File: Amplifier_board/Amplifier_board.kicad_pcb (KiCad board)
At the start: 2 copper layers, 100 x 100 mm, 125 parts, among them J1 Screw Terminal, J10 Conn_01x03_Pin, J11 Conn_01x03_Pin, J12 Conn_01x03_Pin, J13 Conn_01x03_Pin, J14 Conn_01x03_Pin, J15 Conn_01x03_Pin, J2 Screw Terminal, J3 Screw Terminal, J4 Screw Terminal, J5 Screw Terminal, J6 Screw Terminal, J7 A-DF_09_A_KG-T4S, J8 Conn_01x03_Pin, J9 Conn_01x03_Pin, U1 TPA3111D1PWPR, U2 TPA3111D1PWPR, U3 TPA3111D1PWPR, U4 TPA3111D1PWPR

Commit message: More progress on layout
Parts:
- C17, C3, C32, C4, C47: moved to B.Cu
- C28, C29, C43, C44, C54, C58, C60, C61: value 0.5u -> 0.47u
- moved J5 19.0 mm to (162.0, 134.5)
- moved J4 16.0 mm to (137.0, 134.5)
- moved J3 12.5 mm to (112.0, 134.5)
- moved C1 10.2 mm to (88.2, 79.3), turned to 180 degrees
- moved C2 5.91 mm to (88.2, 81.8), turned to 0 degrees
- moved C4 5.46 mm to (84.3, 90.9), turned to 0 degrees
- moved C63 4.20 mm to (215.9, 103.6)
- moved C64 4.20 mm to (199.4, 166.7)
- moved C65 4.20 mm to (269.3, 141.6)
- moved C67 4.20 mm to (210.9, 103.6)
- moved C68 4.20 mm to (194.4, 166.7)
- moved C69 4.20 mm to (264.3, 141.6)
- moved R13 4.00 mm to (84.5, 122.5)
- moved R9 4.00 mm to (89.5, 122.5)
- moved C18 3.21 mm to (212.1, 65.5), turned to -90 degrees
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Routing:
- net +24V: track 0.00 -> 328.3 mm, vias 0 -> 9
- net Net-(U1-INP): track 0.00 -> 12.7 mm
- net Net-(U1-INN): track 0.00 -> 9.94 mm
- net Net-(U4-*FAULT): track 0.00 -> 7.07 mm
- net Net-(U2-*FAULT): track 0.00 -> 7.07 mm
- net Net-(U3-*FAULT): track 0.00 -> 7.07 mm
- net Net-(C61-Pad1): track 0.00 -> 6.03 mm
- net Net-(C44-Pad1): track 0.00 -> 6.03 mm
- net Net-(C29-Pad1): track 0.00 -> 6.03 mm
- net Net-(C58-Pad1): track 0.00 -> 5.98 mm
- net Net-(C54-Pad2): track 0.00 -> 5.98 mm
- net Net-(C28-Pad2): track 0.00 -> 5.98 mm
- net Net-(C43-Pad2): track 0.00 -> 5.98 mm
- net Net-(C60-Pad2): track 0.00 -> 5.98 mm
- net Net-(U3-GVDD): track 0.00 -> 4.85 mm
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
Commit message: More routing on amp board
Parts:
- added JP10: Jumper_1206, Resistor_SMD:R_1206_3216Metric_Pad1.30x1.75mm_HandSolder, F.Cu at (54.0, 60.9)
- added JP11: Jumper_1206, Resistor_SMD:R_1206_3216Metric_Pad1.30x1.75mm_HandSolder, F.Cu at (46.0, 60.9)
- added JP12: Jumper_1206, Resistor_SMD:R_1206_3216Metric_Pad1.30x1.75mm_HandSolder, F.Cu at (46.0, 52.3)
- added JP13: Jumper_1206, Resistor_SMD:R_1206_3216Metric_Pad1.30x1.75mm_HandSolder, F.Cu at (89.0, 79.5)
- added JP14: Jumper_1206, Resistor_SMD:R_1206_3216Metric_Pad1.30x1.75mm_HandSolder, F.Cu at (54.0, 64.2)
- added JP15: Jumper_1206, Resistor_SMD:R_1206_3216Metric_Pad1.30x1.75mm_HandSolder, F.Cu at (46.0, 64.2)
- added JP16: Jumper_1206, Resistor_SMD:R_1206_3216Metric_Pad1.30x1.75mm_HandSolder, F.Cu at (46.0, 55.6)
- added JP9: Jumper_1206, Resistor_SMD:R_1206_3216Metric_Pad1.30x1.75mm_HandSolder, F.Cu at (91.6, 79.5)
- moved C1 6.26 mm to (83.3, 83.2), turned to -90 degrees
- moved C2 3.04 mm to (85.5, 83.2), turned to 90 degrees
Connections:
- J10 pad 2: /amp3/Gain0 -> Net-(J10-Pin_2)
- J11 pad 2: /amp4/Gain0 -> Net-(J11-Pin_2)
- J12 pad 2: /amp1/Gain1 -> Net-(J12-Pin_2)
- J13 pad 2: /amp2/Gain1 -> Net-(J13-Pin_2)
- J14 pad 2: /amp3/Gain1 -> Net-(J14-Pin_2)
- J15 pad 2: /amp4/Gain1 -> Net-(J15-Pin_2)
- J8 pad 2: /amp1/Gain0 -> Net-(J8-Pin_2)
- J9 pad 2: /amp2/Gain0 -> Net-(J9-Pin_2)
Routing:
- net /In1N: track 0.00 -> 46.7 mm
- net /In1P: track 0.00 -> 46.2 mm
- net Net-(J8-Pin_2): track 0.00 -> 11.4 mm
- net /amp1/Gain0: track 0.70 -> 10.9 mm
- net /amp1/Gain1: track 0.01 -> 10.1 mm
- net Net-(U1-INP): track 12.7 -> 6.81 mm
- net Net-(J12-Pin_2): track 0.00 -> 4.79 mm
- net +24V: track 328.3 -> 324.0 mm
- net Net-(U1-INN): track 9.94 -> 6.81 mm
- added copper zone on B.Cu, net GND

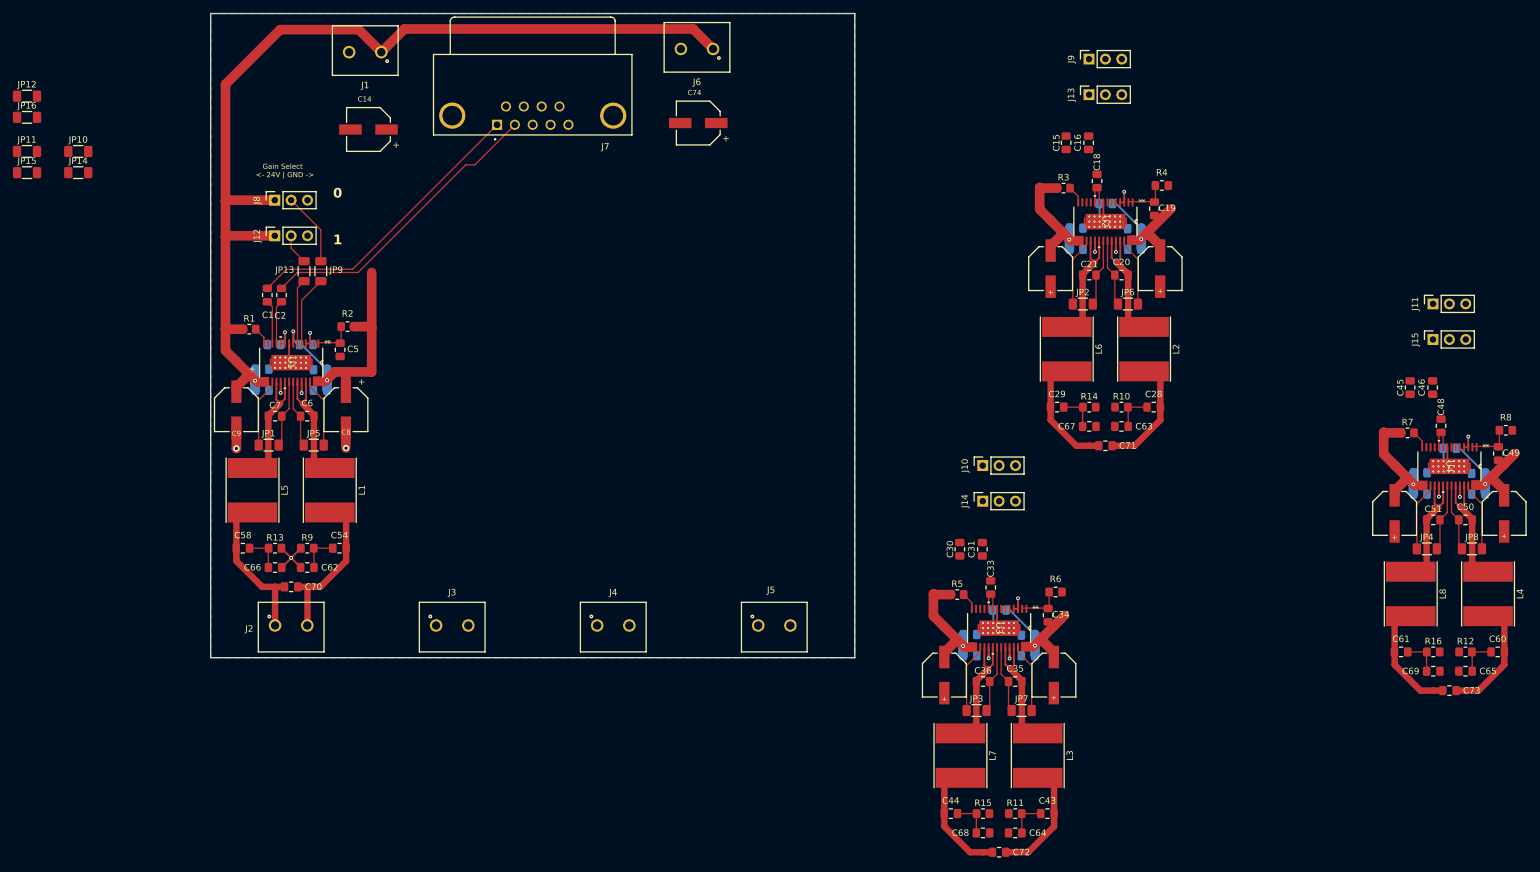
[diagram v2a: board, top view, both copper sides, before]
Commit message: Removed buffers on DAC board
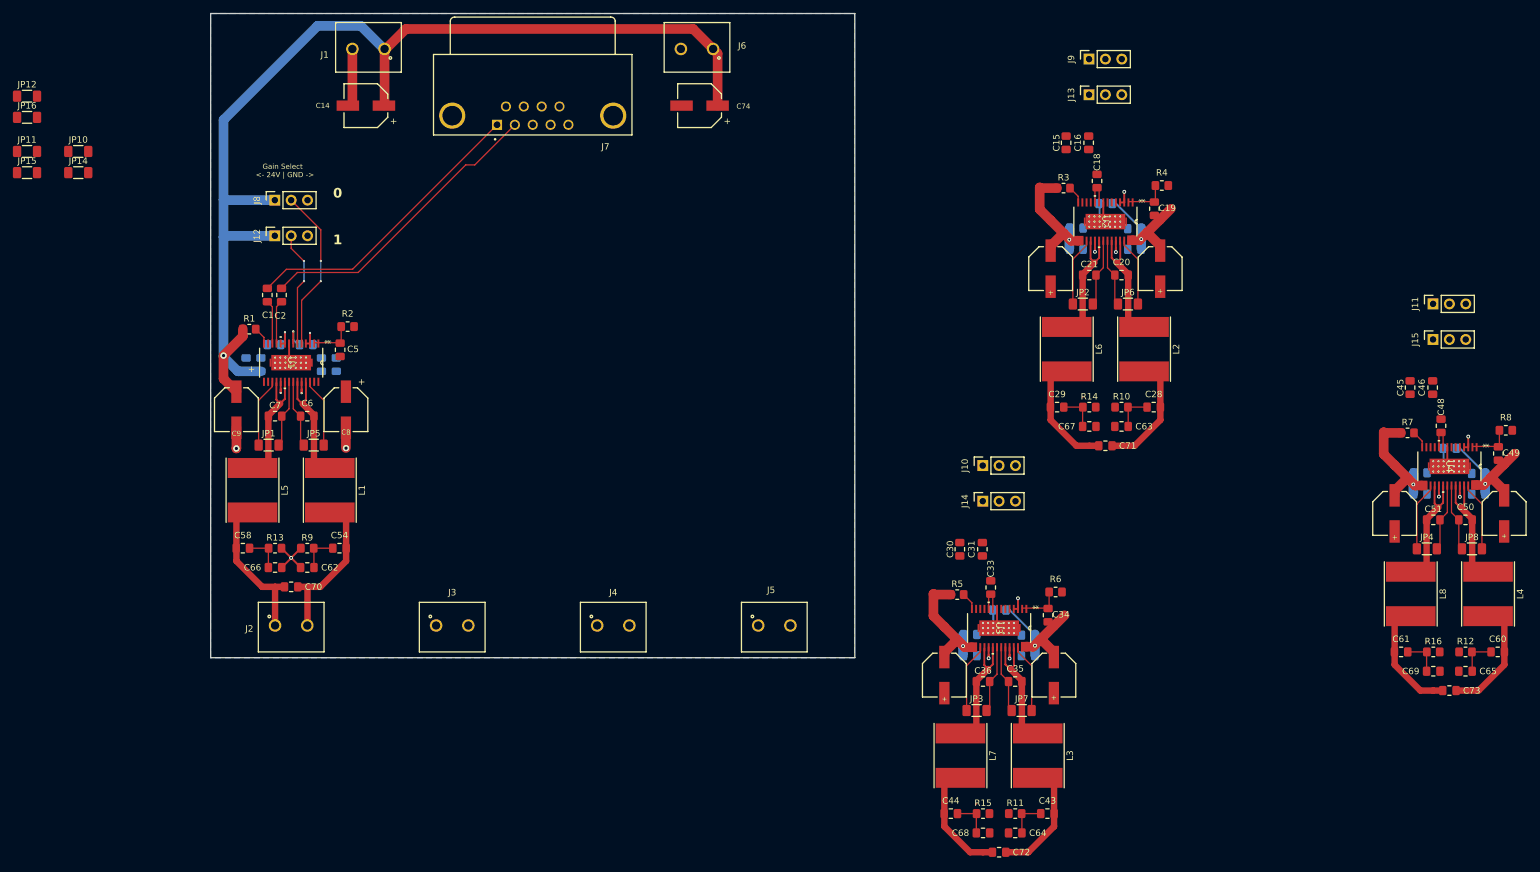
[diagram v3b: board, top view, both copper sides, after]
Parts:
- removed JP13, JP9: Jumper_1206, Resistor_SMD:R_1206_3216Metric_Pad1.30x1.75mm_HandSolder
- moved C12 4.00 mm to (82.3, 94.0), turned to 90 degrees
- moved C13 4.00 mm to (91.7, 94.0), turned to 90 degrees
- moved C14 3.72 mm to (98.6, 53.8)
- moved C74 2.71 mm to (150.4, 53.8)
- moved C11 2.62 mm to (94.0, 94.0), turned to 90 degrees
- moved C10 2.60 mm to (80.0, 94.0), turned to 90 degrees
- moved J1 0.71 mm to (99.0, 45.0)
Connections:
- C74 pad 1: unconnected-(C74-Pad1) -> +24V
- C74 pad 2: unconnected-(C74-Pad2) -> GND
- J10 pad 2: Net-(J10-Pin_2) -> /amp3/Gain0
- J11 pad 2: Net-(J11-Pin_2) -> /amp4/Gain0
- J12 pad 2: Net-(J12-Pin_2) -> /amp1/Gain1
- J13 pad 2: Net-(J13-Pin_2) -> /amp2/Gain1
- J14 pad 2: Net-(J14-Pin_2) -> /amp3/Gain1
- J15 pad 2: Net-(J15-Pin_2) -> /amp4/Gain1
- J8 pad 2: Net-(J8-Pin_2) -> /amp1/Gain0
- J9 pad 2: Net-(J9-Pin_2) -> /amp2/Gain0
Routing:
- net +24V: track 324.0 -> 303.5 mm, vias 9 -> 8
- net /amp1/Gain0: track 10.9 -> 25.4 mm, vias 0 -> 2
- net Net-(J8-Pin_2): track 11.4 -> 0.00 mm
- net GND: track 62.0 -> 70.0 mm
- net /amp1/Gain1: track 10.1 -> 18.0 mm, vias 0 -> 2
- net Net-(J12-Pin_2): track 4.79 -> 0.00 mm

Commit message: Added test points, almost finished layout for amp board
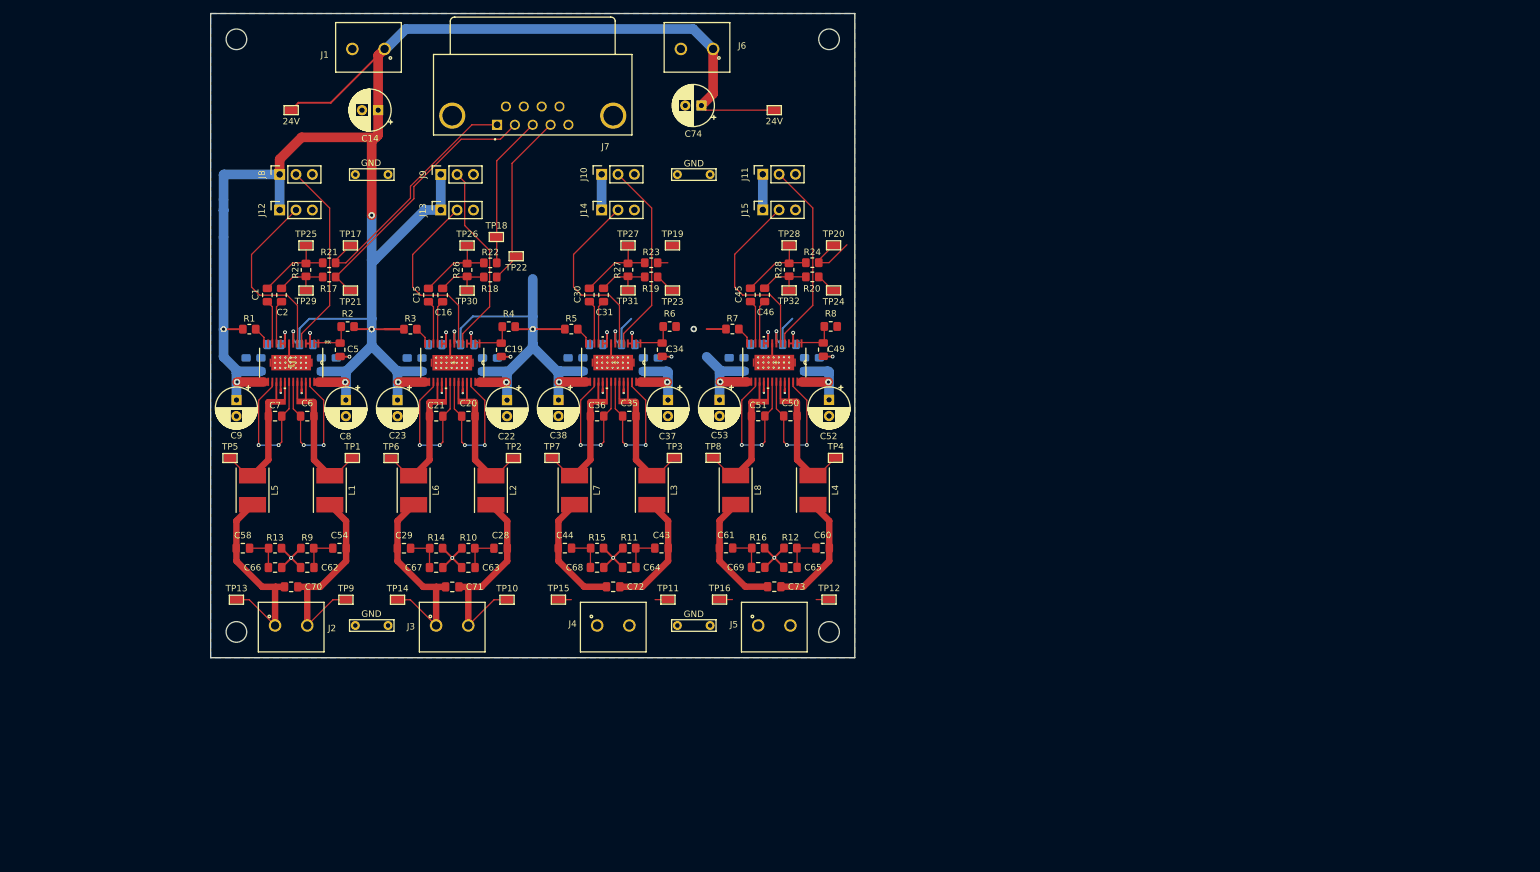
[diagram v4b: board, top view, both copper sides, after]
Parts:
- removed JP1, JP10, JP11, JP12, JP14, JP15, JP16, JP2, JP3, JP4, JP5, JP6, JP7, JP8: Jumper_1206, Resistor_SMD:R_1206_3216Metric_Pad1.30x1.75mm_HandSolder
- added R17: 0, Resistor_SMD:R_0805_2012Metric_Pad1.20x1.40mm_HandSolder, F.Cu at (92.9, 80.4)
- added R18: 0, Resistor_SMD:R_0805_2012Metric_Pad1.20x1.40mm_HandSolder, F.Cu at (117.9, 80.4)
- added R19: 0, Resistor_SMD:R_0805_2012Metric_Pad1.20x1.40mm_HandSolder, F.Cu at (142.9, 80.4)
- added R20: 0, Resistor_SMD:R_0805_2012Metric_Pad1.20x1.40mm_HandSolder, F.Cu at (167.9, 80.4)
- added R21: 0, Resistor_SMD:R_0805_2012Metric_Pad1.20x1.40mm_HandSolder, F.Cu at (92.9, 78.2)
- added R22: 0, Resistor_SMD:R_0805_2012Metric_Pad1.20x1.40mm_HandSolder, F.Cu at (117.9, 78.2)
- added R23: 0, Resistor_SMD:R_0805_2012Metric_Pad1.20x1.40mm_HandSolder, F.Cu at (142.9, 78.2)
- added R24: 0, Resistor_SMD:R_0805_2012Metric_Pad1.20x1.40mm_HandSolder, F.Cu at (167.9, 78.2)
- added R25: omit, Resistor_SMD:R_0805_2012Metric_Pad1.20x1.40mm_HandSolder, F.Cu at (89.3, 79.3)
- added R26: omit, Resistor_SMD:R_0805_2012Metric_Pad1.20x1.40mm_HandSolder, F.Cu at (114.3, 79.3)
- added R27: omit, Resistor_SMD:R_0805_2012Metric_Pad1.20x1.40mm_HandSolder, F.Cu at (139.3, 79.3)
- added R28: omit, Resistor_SMD:R_0805_2012Metric_Pad1.20x1.40mm_HandSolder, F.Cu at (164.3, 79.3)
- added TP1: N, project_lib:TP_RCUCTE, F.Cu at (96.5, 108.5)
- added TP10: OutN, project_lib:TP_RCUCTE, F.Cu at (120.5, 130.5)
- added TP11: OutN, project_lib:TP_RCUCTE, F.Cu at (145.5, 130.5)
- added TP12: OutN, project_lib:TP_RCUCTE, F.Cu at (170.5, 130.5)
- added TP13: OutP, project_lib:TP_RCUCTE, F.Cu at (78.5, 130.5)
- added TP14: OutP, project_lib:TP_RCUCTE, F.Cu at (103.5, 130.5)
- added TP15: OutP, project_lib:TP_RCUCTE, F.Cu at (128.5, 130.5)
- added TP16: OutP, project_lib:TP_RCUCTE, F.Cu at (153.5, 130.5)
- added TP17: InP, project_lib:TP_RCUCTE, F.Cu at (96.2, 75.5)
- added TP18: InP, project_lib:TP_RCUCTE, F.Cu at (118.8, 74.2)
- added TP19: InP, project_lib:TP_RCUCTE, F.Cu at (146.2, 75.5)
- added TP2: N, project_lib:TP_RCUCTE, F.Cu at (121.5, 108.5)
- added TP20: InP, project_lib:TP_RCUCTE, F.Cu at (171.2, 75.5)
- added TP21: InN, project_lib:TP_RCUCTE, F.Cu at (96.2, 82.5)
- added TP22: InN, project_lib:TP_RCUCTE, F.Cu at (121.9, 77.2)
- added TP23: InN, project_lib:TP_RCUCTE, F.Cu at (146.2, 82.5)
- added TP24: InN, project_lib:TP_RCUCTE, F.Cu at (171.2, 82.5)
- added TP25: P, project_lib:TP_RCUCTE, F.Cu at (89.3, 75.5)
- added TP26: P, project_lib:TP_RCUCTE, F.Cu at (114.3, 75.5)
- added TP27: P, project_lib:TP_RCUCTE, F.Cu at (139.3, 75.5)
- added TP28: P, project_lib:TP_RCUCTE, F.Cu at (164.3, 75.5)
- added TP29: N, project_lib:TP_RCUCTE, F.Cu at (89.3, 82.5)
- added TP3: N, project_lib:TP_RCUCTE, F.Cu at (146.5, 108.5)
- added TP30: N, project_lib:TP_RCUCTE, F.Cu at (114.3, 82.5)
- added TP31: N, project_lib:TP_RCUCTE, F.Cu at (139.3, 82.5)
- added TP32: N, project_lib:TP_RCUCTE, F.Cu at (164.3, 82.5)
- added TP33: 24V, project_lib:TP_RCUCTE, F.Cu at (87.0, 54.5)
- added TP34: 24V, project_lib:TP_RCUCTE, F.Cu at (162.0, 54.5)
- added TP35: GND, TestPoint:TestPoint_Bridge_Pitch5.08mm_Drill0.7mm, F.Cu at (97.0, 64.5)
- added TP36: GND, TestPoint:TestPoint_Bridge_Pitch5.08mm_Drill0.7mm, F.Cu at (97.0, 134.5)
- added TP37: GND, TestPoint:TestPoint_Bridge_Pitch5.08mm_Drill0.7mm, F.Cu at (147.0, 64.5)
- added TP38: GND, TestPoint:TestPoint_Bridge_Pitch5.08mm_Drill0.7mm, F.Cu at (147.0, 134.5)
- added TP4: N, project_lib:TP_RCUCTE, F.Cu at (171.5, 108.5)
- added TP5: P, project_lib:TP_RCUCTE, F.Cu at (77.5, 108.5)
- added TP6: P, project_lib:TP_RCUCTE, F.Cu at (102.5, 108.5)
- added TP7: P, project_lib:TP_RCUCTE, F.Cu at (127.5, 108.5)
- added TP8: P, project_lib:TP_RCUCTE, F.Cu at (152.5, 108.5)
- added TP9: OutN, project_lib:TP_RCUCTE, F.Cu at (95.5, 130.5)
- C14, C22, C23, C37, C38, C52, C53, C74, C8, C9: footprint project_lib:WCAP-ASLI_6.3X7.7_DXL_ -> Capacitor_THT:CP_Radial_D6.3mm_P2.50mm
- C18, C33, C48: moved to B.Cu
- C28, C29, C43, C44, C54, C58, C60, C61: value 0.47u -> 2.2u
- C62, C63, C64, C65, C66, C67, C68, C69: value C_Small -> omit
- L1, L2, L3, L4, L5, L6, L7, L8: value 68u -> 15u; footprint Inductor_SMD:L_Taiyo-Yuden_NR-80xx_HandSoldering -> Inductor_SMD:L_Taiyo-Yuden_NR-50xx_HandSoldering
- moved C55 108.6 mm to (155.0, 94.0), turned to 90 degrees
- moved C57 106.9 mm to (157.3, 94.0), turned to 90 degrees
- moved C48 106.9 mm to (159.3, 90.9), turned to 0 degrees
- moved C59 106.5 mm to (166.7, 94.0), turned to 90 degrees
- moved C52 106.3 mm to (170.5, 99.5), turned to -90 degrees
- moved C53 106.3 mm to (153.5, 99.5), turned to -90 degrees
- moved C50 106.0 mm to (164.5, 102.0)
- moved C51 106.0 mm to (159.5, 102.0)
- moved C61 106.0 mm to (154.5, 122.5)
- moved L8 106.0 mm to (156.0, 113.5)
- moved C60 106.0 mm to (169.5, 122.5)
- moved C65 106.0 mm to (164.5, 125.5)
- moved C69 106.0 mm to (159.5, 125.5)
- moved C73 106.0 mm to (162.0, 128.5)
- moved L4 106.0 mm to (168.0, 113.5)
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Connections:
- C1 pad 1: /In1P -> Net-(C1-Pad1)
- C15 pad 1: /In2P -> Net-(C15-Pad1)
- C16 pad 2: /In2N -> Net-(C16-Pad2)
- C2 pad 2: /In1N -> Net-(C2-Pad2)
- C20 pad 2: Net-(JP6-A) -> Net-(C20-Pad2)
- C21 pad 2: Net-(JP2-B) -> Net-(C21-Pad2)
- C30 pad 1: /In3P -> Net-(C30-Pad1)
- C31 pad 2: /In3N -> Net-(C31-Pad2)
- C35 pad 2: Net-(JP7-A) -> Net-(C35-Pad2)
- C36 pad 2: Net-(JP3-B) -> Net-(C36-Pad2)
- C45 pad 1: /In4P -> Net-(C45-Pad1)
- C46 pad 2: /In4N -> Net-(C46-Pad2)
- C50 pad 2: Net-(JP8-A) -> Net-(C50-Pad2)
- C51 pad 2: Net-(JP4-B) -> Net-(C51-Pad2)
- C6 pad 2: Net-(JP5-A) -> Net-(C6-Pad2)
- C7 pad 2: Net-(JP1-B) -> Net-(C7-Pad2)
- U1 pad 17: Net-(JP1-A) -> Net-(C7-Pad2)
- U1 pad 21: Net-(JP1-B) -> Net-(C7-Pad2)
- U1 pad 22: Net-(JP5-A) -> Net-(C6-Pad2)
- U1 pad 26: Net-(JP5-B) -> Net-(C6-Pad2)
- U2 pad 17: Net-(JP2-A) -> Net-(C21-Pad2)
- U2 pad 21: Net-(JP2-B) -> Net-(C21-Pad2)
- U2 pad 22: Net-(JP6-A) -> Net-(C20-Pad2)
- U2 pad 26: Net-(JP6-B) -> Net-(C20-Pad2)
- U3 pad 17: Net-(JP3-A) -> Net-(C36-Pad2)
- U3 pad 21: Net-(JP3-B) -> Net-(C36-Pad2)
- U3 pad 22: Net-(JP7-A) -> Net-(C35-Pad2)
- U3 pad 26: Net-(JP7-B) -> Net-(C35-Pad2)
- U4 pad 17: Net-(JP4-A) -> Net-(C51-Pad2)
- U4 pad 21: Net-(JP4-B) -> Net-(C51-Pad2)
- U4 pad 22: Net-(JP8-A) -> Net-(C50-Pad2)
- U4 pad 26: Net-(JP8-B) -> Net-(C50-Pad2)
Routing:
- net +24V: track 303.5 -> 455.1 mm, vias 8 -> 17
- net /amp4/Gain0: track 0.00 -> 30.2 mm
- net /amp3/Gain0: track 0.00 -> 30.2 mm
- net /amp2/Gain0: track 0.00 -> 30.1 mm
- net /amp4/Gain1: track 0.00 -> 29.0 mm
- net /amp2/Gain1: track 0.00 -> 29.0 mm
- net /amp3/Gain1: track 0.00 -> 29.0 mm
- net /In2N: track 0.00 -> 27.2 mm
- net Net-(C51-Pad2): track 0.00 -> 24.5 mm, vias 0 -> 2
- net Net-(C21-Pad2): track 0.00 -> 24.5 mm, vias 0 -> 2
- net Net-(C36-Pad2): track 0.00 -> 24.5 mm, vias 0 -> 2
- net Net-(C7-Pad2): track 0.00 -> 24.5 mm, vias 0 -> 2
- net Net-(C50-Pad2): track 0.00 -> 24.3 mm, vias 0 -> 2
- net Net-(C20-Pad2): track 0.00 -> 24.3 mm, vias 0 -> 2
- net Net-(C6-Pad2): track 0.00 -> 24.3 mm, vias 0 -> 2
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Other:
- outline, holes or cut-outs redrawn
- board text removed: "0 1"
- board text removed: "Gain Select <- 24V | GND ->"
